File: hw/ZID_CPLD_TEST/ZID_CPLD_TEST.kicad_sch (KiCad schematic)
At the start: 9 parts

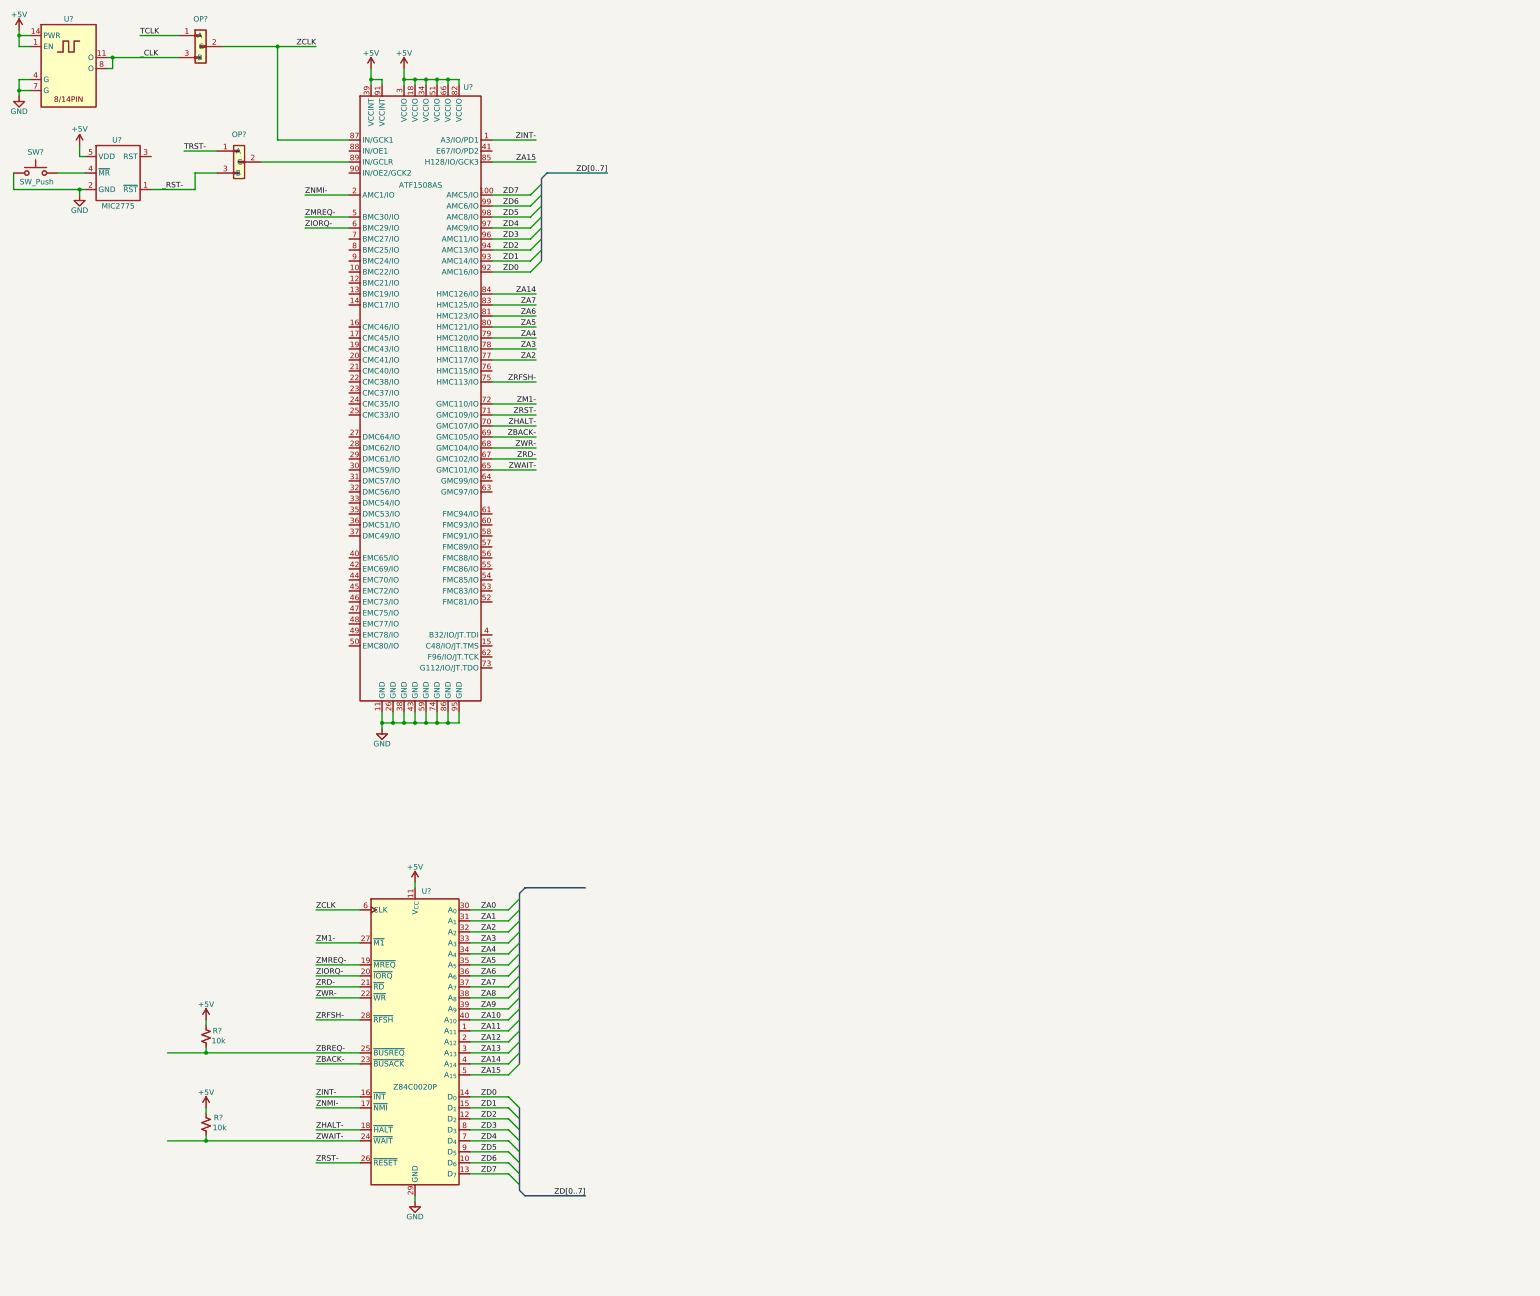
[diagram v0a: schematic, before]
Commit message: CPLD: zsr, mmu, sbcgp, dbi working
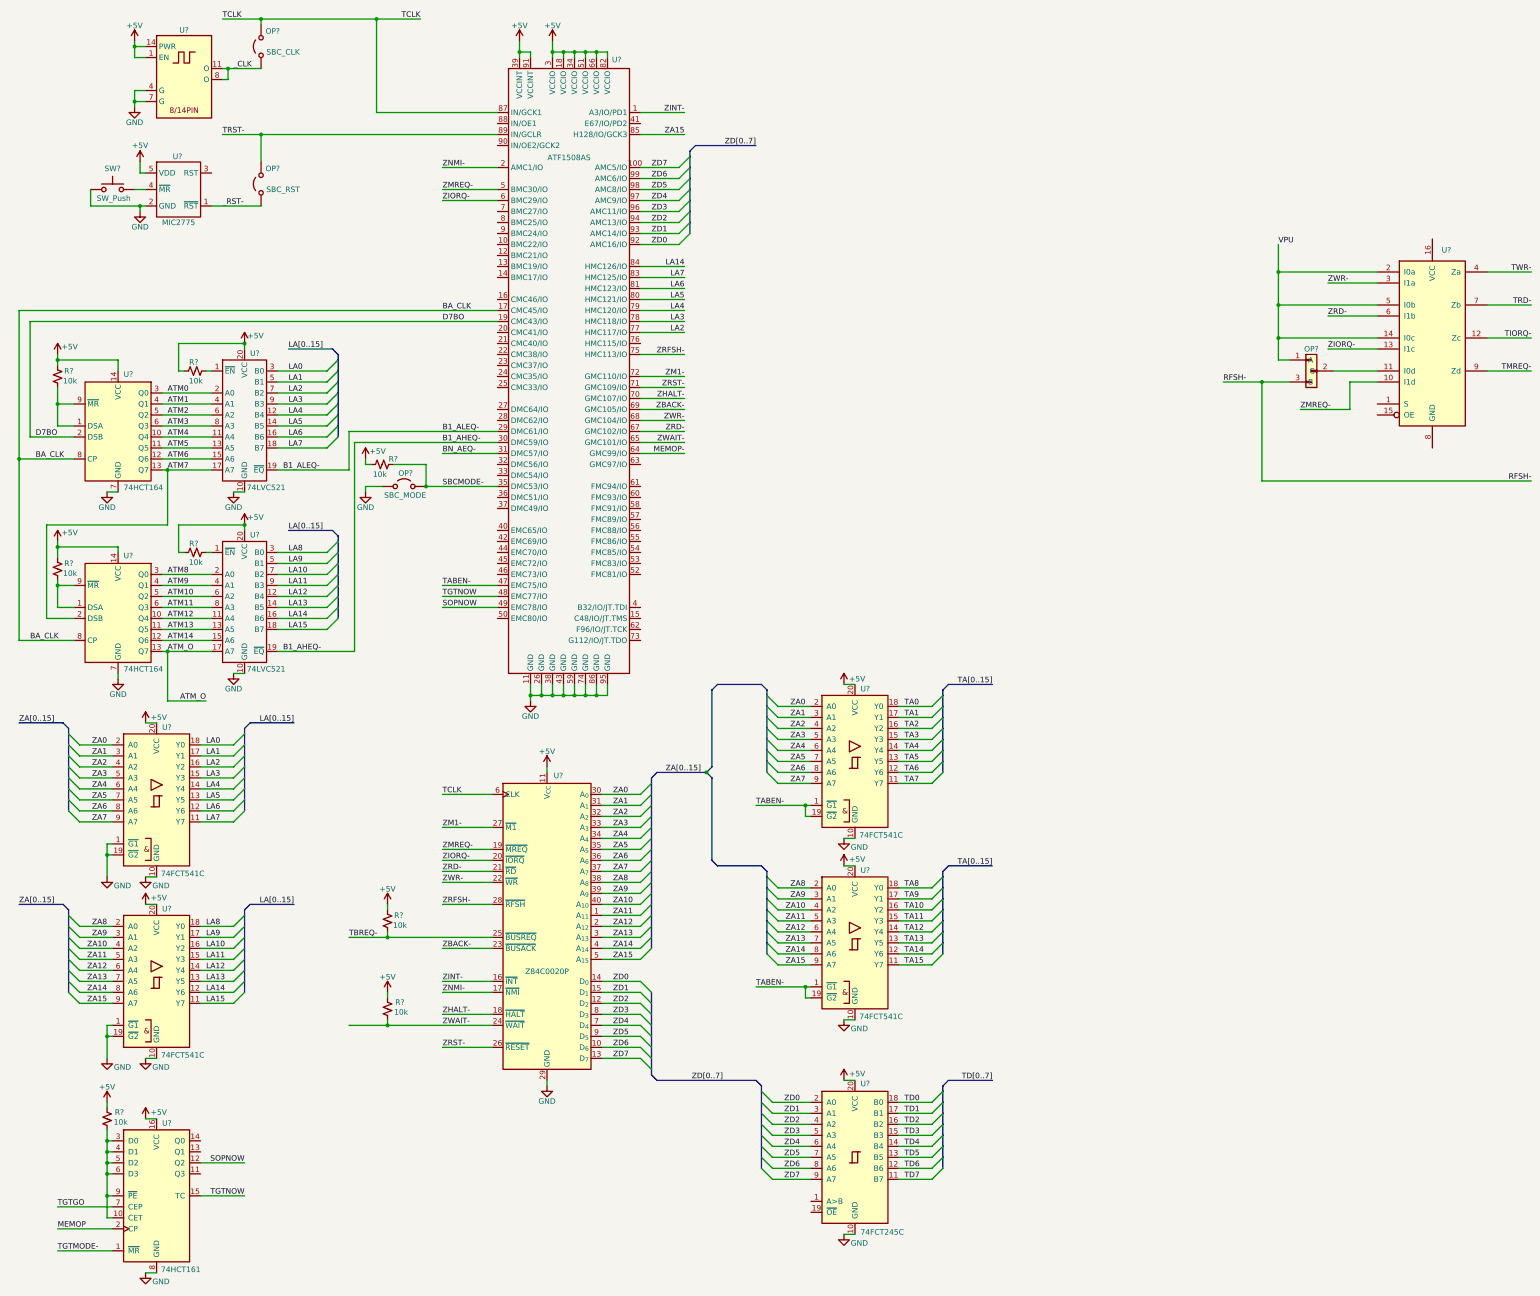
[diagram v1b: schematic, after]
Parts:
- removed OP? (x2): AES-Option_A-B_2mm, Connector_PinHeader_2.00mm:PinHeader_1x03_P2.00mm_Vertical, symbol AES_Library:AES-Option_A-B_2mm
- added OP?: AES-Option_A-B_2mm, Connector_PinHeader_2.00mm:PinHeader_1x03_P2.00mm_Vertical, symbol AES_Library:AES-Option_A-B_2mm
- added OP? (x3): 1x02 2.0mm, symbol Jumper:Jumper_2_Open
- added R? (x6): 10k, symbol Device:R_Small_US
- added U? (x4): 74FCT541C, symbol AES_Library:74541-AES
- added U?: ~, symbol 74xx:74LS257
- added U? (x2): 74HCT164, symbol 74xx:74HCT164
- added U?: 74HCT161, symbol AES_Library:74161-AES
- added U?: 74FCT245C, symbol AES_Library:74245-AES
- added U? (x2): 74LVC521, Package_SO:SOIC-20W_7.5x12.8mm_P1.27mm, symbol AES_Library:74521-AES
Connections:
- net ZCLK is gone; now on net TCLK: U?.6 (CLK), U?.87 (IN/GCK1)
- net +5V: now also R?.1, R?.1, R?.1, R?.1, R?.1, R?.1, U?.14 (VCC), U?.14 (VCC), U?.16 (VCC), U?.20 (VCC), U?.20 (VCC), U?.20 (VCC), U?.20 (VCC), U?.20 (VCC), U?.20 (VCC), U?.20 (VCC)
- net GND: now also OP?.1 (A), U?.1 (~{G1}), U?.1 (~{G1}), U?.10 (GND), U?.10 (GND), U?.10 (GND), U?.10 (GND), U?.10 (GND), U?.10 (GND), U?.10 (GND), U?.19 (~{G2}), U?.19 (~{G2}), U?.7 (GND), U?.7 (GND), U?.8 (GND)
- net TCLK: now also OP?.2 (B)
- net TRST-: now also U?.89 (IN/GCLR), OP?.2 (B)
- net ZA0: now also U?.2 (A0), U?.2 (A0)
- net ZA1: now also U?.3 (A1), U?.3 (A1)
- net ZA10: now also U?.4 (A2), U?.4 (A2)
- net ZA11: now also U?.5 (A3), U?.5 (A3)
- net ZA12: now also U?.6 (A4), U?.6 (A4)
- net ZA13: now also U?.7 (A5), U?.7 (A5)
- net ZA14: now also U?.8 (A6), U?.8 (A6); no longer U?.84 (HMC126/IO)
- net ZA15: now also U?.9 (A7), U?.9 (A7)
- net ZA2: now also U?.4 (A2), U?.4 (A2); no longer U?.77 (HMC117/IO)
- net ZA3: now also U?.5 (A3), U?.5 (A3); no longer U?.78 (HMC118/IO)
- net ZA4: now also U?.6 (A4), U?.6 (A4); no longer U?.79 (HMC120/IO)
- net ZA5: now also U?.7 (A5), U?.7 (A5); no longer U?.80 (HMC121/IO)
- net ZA6: now also U?.8 (A6), U?.8 (A6); no longer U?.81 (HMC123/IO)
- net ZA7: now also U?.9 (A7), U?.9 (A7); no longer U?.83 (HMC125/IO)
- net ZA8: now also U?.2 (A0), U?.2 (A0)
- net ZA9: now also U?.3 (A1), U?.3 (A1)
- net ZD0: now also U?.2 (A0)
- net ZD1: now also U?.3 (A1)
- net ZD2: now also U?.4 (A2)
- net ZD3: now also U?.5 (A3)
- net ZD4: now also U?.6 (A4)
- net ZD5: now also U?.7 (A5)
- net ZD6: now also U?.8 (A6)
- net ZD7: now also U?.9 (A7)
- net ZIORQ-: now also U?.13 (I1c)
- net ZMREQ-: now also U?.10 (I1d)
- net ZRD-: now also U?.6 (I1b)
- net ZWR-: now also U?.3 (I1a)
- net _CLK: now also OP?.1 (A)
- net _RST-: now also OP?.1 (A)
- net BA_CLK: now reaches U?.17 (CMC45/IO)
- net BA_CLK: now also U?.8 (CP), U?.8 (CP)
- net D7BO: now reaches U?.19 (CMC43/IO)
- net D7BO: now also U?.2 (DSB)
- net B1_ALEQ-: now reaches U?.29 (DMC61/IO)
- net B1_ALEQ-: now also U?.19 (~{EQ})
- net B1_AHEQ-: now reaches U?.30 (DMC59/IO)
- net B1_AHEQ-: now also U?.19 (~{EQ})
- net BN_AEQ-: now reaches U?.31 (DMC57/IO)
- net SBCMODE-: now reaches U?.35 (DMC53/IO)
- net SBCMODE-: now also OP?.2 (B), R?.2
- net TABEN-: now reaches U?.47 (EMC75/IO)
- net TABEN-: now also U?.1 (~{G1}), U?.1 (~{G1}), U?.19 (~{G2}), U?.19 (~{G2})
- net TGTNOW: now reaches U?.48 (EMC77/IO)
- net TGTNOW: now also U?.15 (TC)
- net SOPNOW: now reaches U?.49 (EMC78/IO)
- net SOPNOW: now also U?.12 (Q2)
- net MEMOP-: now reaches U?.64 (GMC99/IO)
- net ZBREQ- renamed TBREQ-
- new net: OP?.2 (C), U?.11 (I0d)
- new net: R?.2, U?.1 (DSA), U?.9 (~{MR}) (x2)
- new net: R?.2, U?.1 (~{EN}) (x2)
- new net: R?.2, U?.10 (CET), U?.3 (D0), U?.4 (D1), U?.5 (D2), U?.6 (D3), U?.9 (~{PE})
- new net ATM0: U?.2 (A0), U?.3 (Q0)
- new net ATM1: U?.4 (A1), U?.4 (Q1)
- new net ATM10: U?.5 (Q2), U?.6 (A2)
- new net ATM11: U?.6 (Q3), U?.8 (A3)
- new net ATM12: U?.10 (Q4), U?.11 (A4)
- new net ATM13: U?.11 (Q5), U?.13 (A5)
- new net ATM14: U?.12 (Q6), U?.15 (A6)
- new net ATM2: U?.5 (Q2), U?.6 (A2)
- new net ATM3: U?.6 (Q3), U?.8 (A3)
- new net ATM4: U?.10 (Q4), U?.11 (A4)
- new net ATM5: U?.11 (Q5), U?.13 (A5)
- new net ATM6: U?.12 (Q6), U?.15 (A6)
- new net ATM7: U?.13 (Q7), U?.17 (A7), U?.2 (DSB)
- new net ATM8: U?.2 (A0), U?.3 (Q0)
- new net ATM9: U?.4 (A1), U?.4 (Q1)
- new net ATM_O: U?.13 (Q7), U?.17 (A7)
- new net LA0: U?.18 (Y0), U?.3 (B0)
- new net LA1: U?.17 (Y1), U?.5 (B1)
- new net LA10: U?.16 (Y2), U?.7 (B2)
- new net LA11: U?.15 (Y3), U?.9 (B3)
- new net LA12: U?.12 (B4), U?.14 (Y4)
- new net LA13: U?.13 (Y5), U?.14 (B5)
- new net LA14: U?.12 (Y6), U?.16 (B6), U?.84 (HMC126/IO)
- new net LA15: U?.11 (Y7), U?.18 (B7)
- new net LA2: U?.16 (Y2), U?.7 (B2), U?.77 (HMC117/IO)
- new net LA3: U?.15 (Y3), U?.78 (HMC118/IO), U?.9 (B3)
- new net LA4: U?.12 (B4), U?.14 (Y4), U?.79 (HMC120/IO)
- new net LA5: U?.13 (Y5), U?.14 (B5), U?.80 (HMC121/IO)
- new net LA6: U?.12 (Y6), U?.16 (B6), U?.81 (HMC123/IO)
- new net LA7: U?.11 (Y7), U?.18 (B7), U?.83 (HMC125/IO)
- new net LA8: U?.18 (Y0), U?.3 (B0)
- new net LA9: U?.17 (Y1), U?.5 (B1)
- new net MEMOP: U?.2 (CP)
- new net RFSH-: OP?.3 (B)
- new net TA0: U?.18 (Y0)
- new net TA1: U?.17 (Y1)
- new net TA10: U?.16 (Y2)
- new net TA11: U?.15 (Y3)
- new net TA12: U?.14 (Y4)
- new net TA13: U?.13 (Y5)
- new net TA14: U?.12 (Y6)
- new net TA15: U?.11 (Y7)
- new net TA2: U?.16 (Y2)
- new net TA3: U?.15 (Y3)
- new net TA4: U?.14 (Y4)
- new net TA5: U?.13 (Y5)
- new net TA6: U?.12 (Y6)
- new net TA7: U?.11 (Y7)
- new net TA8: U?.18 (Y0)
- new net TA9: U?.17 (Y1)
- new net TD0: U?.18 (B0)
- new net TD1: U?.17 (B1)
- new net TD2: U?.16 (B2)
- new net TD3: U?.15 (B3)
- new net TD4: U?.14 (B4)
- new net TD5: U?.13 (B5)
- new net TD6: U?.12 (B6)
- new net TD7: U?.11 (B7)
- new net TGTGO: U?.7 (CEP)
- new net TGTMODE-: U?.1 (~{MR})
- new net TIORQ-: U?.12 (Zc)
- new net TMREQ-: U?.9 (Zd)
- new net TRD-: U?.7 (Zb)
- new net TWR-: U?.4 (Za)
- new net VPU: OP?.1 (A), U?.14 (I0c), U?.2 (I0a), U?.5 (I0b)
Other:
- title: ZID CPLD Test -> ZID - Z80 In-circuit Debugger
- moved on the sheet: R?, SW?, U?

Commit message: CPLD tested break and reset
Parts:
- removed U? (x2): 74FCT541C, symbol AES_Library:74541-AES
- added U? (x2): 74FCT2245, symbol AES_Library:74245-AES
- added U?: 74AHCT244, symbol AES_Library:74244_OI-AES
- added U?: 74FCT541C, symbol AES_Library:74541-AES
- U?: value ~ -> 74FCT257T
- U?: value 74FCT245C -> 74FCT2245
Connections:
- net +5V: now also U?.16 (VCC), U?.20 (VCC), U?.20 (VCC), U?.20 (VCC)
- net B1_AHEQ-: no longer U?.30 (DMC59/IO)
- net B1_ALEQ-: no longer U?.29 (DMC61/IO)
- net BA_CLK: no longer U?.17 (CMC45/IO)
- net BN_AEQ-: now also U?.7 (BMC27/IO); no longer U?.31 (DMC57/IO)
- net D7BO: no longer U?.19 (CMC43/IO)
- net GND: now also U?.8 (GND), U?.10 (GND), U?.10 (GND), U?.10 (GND)
- net MEMOP-: now also U?.31 (DMC57/IO); no longer U?.64 (GMC99/IO)
- net SBCMODE-: now also U?.32 (DMC56/IO); no longer U?.35 (DMC53/IO)
- net SOPNOW: now also U?.47 (EMC75/IO); no longer U?.49 (EMC78/IO)
- net TA0: now also U?.18 (B0)
- net TA1: now also U?.17 (B1)
- net TA10: now also U?.16 (B2)
- net TA11: now also U?.15 (B3)
- net TA12: now also U?.14 (B4)
- net TA13: now also U?.13 (B5)
- net TA14: now also U?.12 (B6)
- net TA15: now also U?.11 (B7)
- net TA2: now also U?.16 (B2)
- net TA3: now also U?.15 (B3)
- net TA4: now also U?.14 (B4)
- net TA5: now also U?.13 (B5)
- net TA6: now also U?.12 (B6)
- net TA7: now also U?.11 (B7)
- net TA8: now also U?.18 (B0)
- net TA9: now also U?.17 (B1)
- net TABEN-: no longer U?.47 (EMC75/IO)
- net TIORQ-: now also U?.6 (I2a)
- net TMREQ-: now also U?.8 (I3a)
- net TRD-: now also U?.4 (I1a)
- net TWR-: now also U?.2 (I0a)
- net ZA0: now also U?.2 (A0)
- net ZA1: now also U?.3 (A1)
- net ZA10: now also U?.4 (A2)
- net ZA11: now also U?.5 (A3)
- net ZA12: now also U?.6 (A4)
- net ZA13: now also U?.7 (A5)
- net ZA14: now also U?.8 (A6)
- net ZA15: now also U?.9 (A7)
- net ZA2: now also U?.4 (A2)
- net ZA3: now also U?.5 (A3)
- net ZA4: now also U?.6 (A4)
- net ZA5: now also U?.7 (A5)
- net ZA6: now also U?.8 (A6)
- net ZA7: now also U?.9 (A7)
- net ZA8: now also U?.2 (A0)
- net ZA9: now also U?.3 (A1)
- net ZBACK-: now also U?.65 (GMC101/IO); no longer U?.69 (GMC105/IO)
- net ZD0: now also U?.16 (CMC46/IO); no longer U?.92 (AMC16/IO)
- net ZD1: now also U?.17 (CMC45/IO); no longer U?.93 (AMC14/IO)
- net ZD2: now also U?.19 (CMC43/IO); no longer U?.94 (AMC13/IO)
- net ZD3: now also U?.20 (CMC41/IO); no longer U?.96 (AMC11/IO)
- net ZD4: now also U?.21 (CMC40/IO); no longer U?.97 (AMC9/IO)
- net ZD5: now also U?.22 (CMC38/IO); no longer U?.98 (AMC8/IO)
- net ZD6: now also U?.23 (CMC37/IO); no longer U?.99 (AMC6/IO)
- net ZD7: now also U?.24 (CMC35/IO); no longer U?.100 (AMC5/IO)
- net ZHALT-: no longer U?.70 (GMC107/IO)
- net ZIORQ-: now also U?.69 (GMC105/IO), U?.14 (O2a); no longer U?.6 (BMC29/IO)
- net ZM1-: now also U?.90 (IN/OE2/GCK2); no longer U?.72 (GMC110/IO)
- net ZMREQ-: now also U?.70 (GMC107/IO), U?.12 (O3a); no longer U?.5 (BMC30/IO)
- net ZRD-: now also U?.16 (O1a)
- net ZRFSH-: now also U?.72 (GMC110/IO); no longer U?.75 (HMC113/IO)
- net ZRST-: now also U?.25 (CMC33/IO), U?.19 (~{OE}), U?.19 (~{OE}); no longer U?.71 (GMC109/IO)
- net ZWAIT-: now also U?.64 (GMC99/IO); no longer U?.65 (GMC101/IO)
- net ZWR-: now also U?.18 (O0a)
- net TGTMODE: now reaches U?.1 (S)
- net BUSACK_H: now reaches U?.15 (OE)
- net SBC_GPI3: now reaches U?.52 (FMC81/IO)
- net SBC_GPI2: now reaches U?.53 (FMC83/IO)
- net SBC_GPI1: now reaches U?.54 (FMC85/IO)
- net SBC_GPI0: now reaches U?.55 (FMC86/IO)
- net SBC_GPO3: now reaches U?.56 (FMC88/IO)
- net SBC_GPO2: now reaches U?.57 (FMC89/IO)
- net SBC_GPO1: now reaches U?.58 (FMC91/IO)
- net SBC_GPO0: now reaches U?.60 (FMC93/IO)
- net TDBUSIN-: now reaches U?.1 (A>B)
- net TDBUSEN-: now reaches U?.19 (~{OE})
- new net BUSACKL-: U?.1 (A>B), U?.1 (A>B)
- new net BUSACK_L-: U?.1 (~{OEa})
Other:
- moved on the sheet: OP?, U?

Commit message: CPLD: Pins assigned
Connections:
- net VPU: now also U?.13 (I1c), U?.3 (I1a), U?.6 (I1b); no longer U?.14 (I0c), U?.2 (I0a), U?.5 (I0b)
- net ZIORQ-: now also U?.14 (I0c); no longer U?.13 (I1c)
- net ZMREQ-: now also U?.11 (I0d); no longer U?.10 (I1d)
- net ZRD-: now also U?.5 (I0b); no longer U?.6 (I1b)
- net ZWR-: now also U?.2 (I0a); no longer U?.3 (I1a)
- net at OP?.2 (C): now also U?.10 (I1d); no longer U?.11 (I0d)
- net TGTMODE renamed FIXED_SEL
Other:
- moved on the sheet: OP?, R?, U?
